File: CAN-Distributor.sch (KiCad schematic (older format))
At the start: 1 part

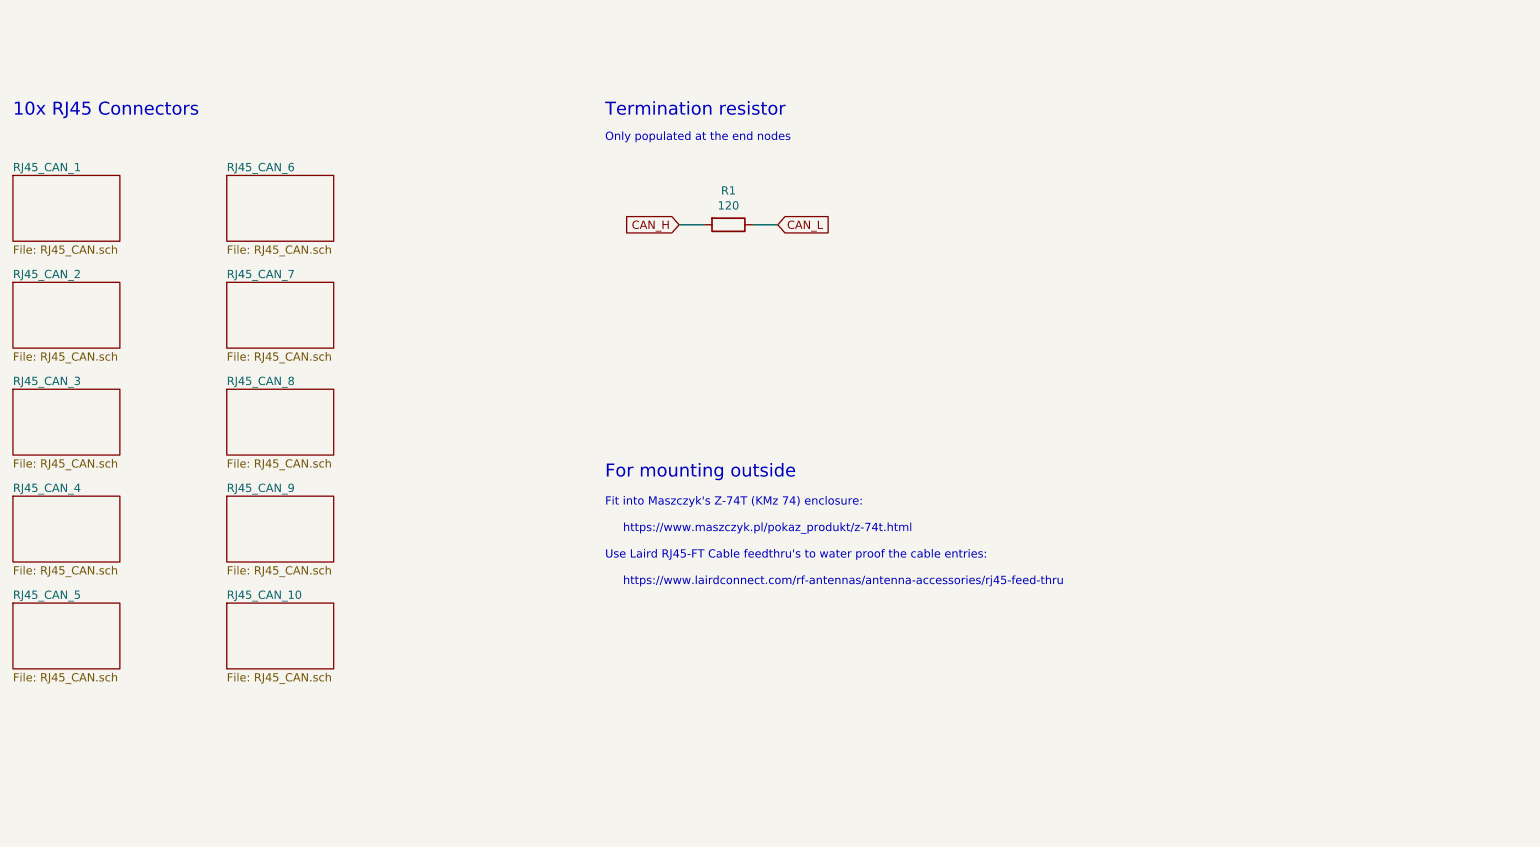
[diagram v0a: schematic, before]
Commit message: Design v2 circuit and make footprints.
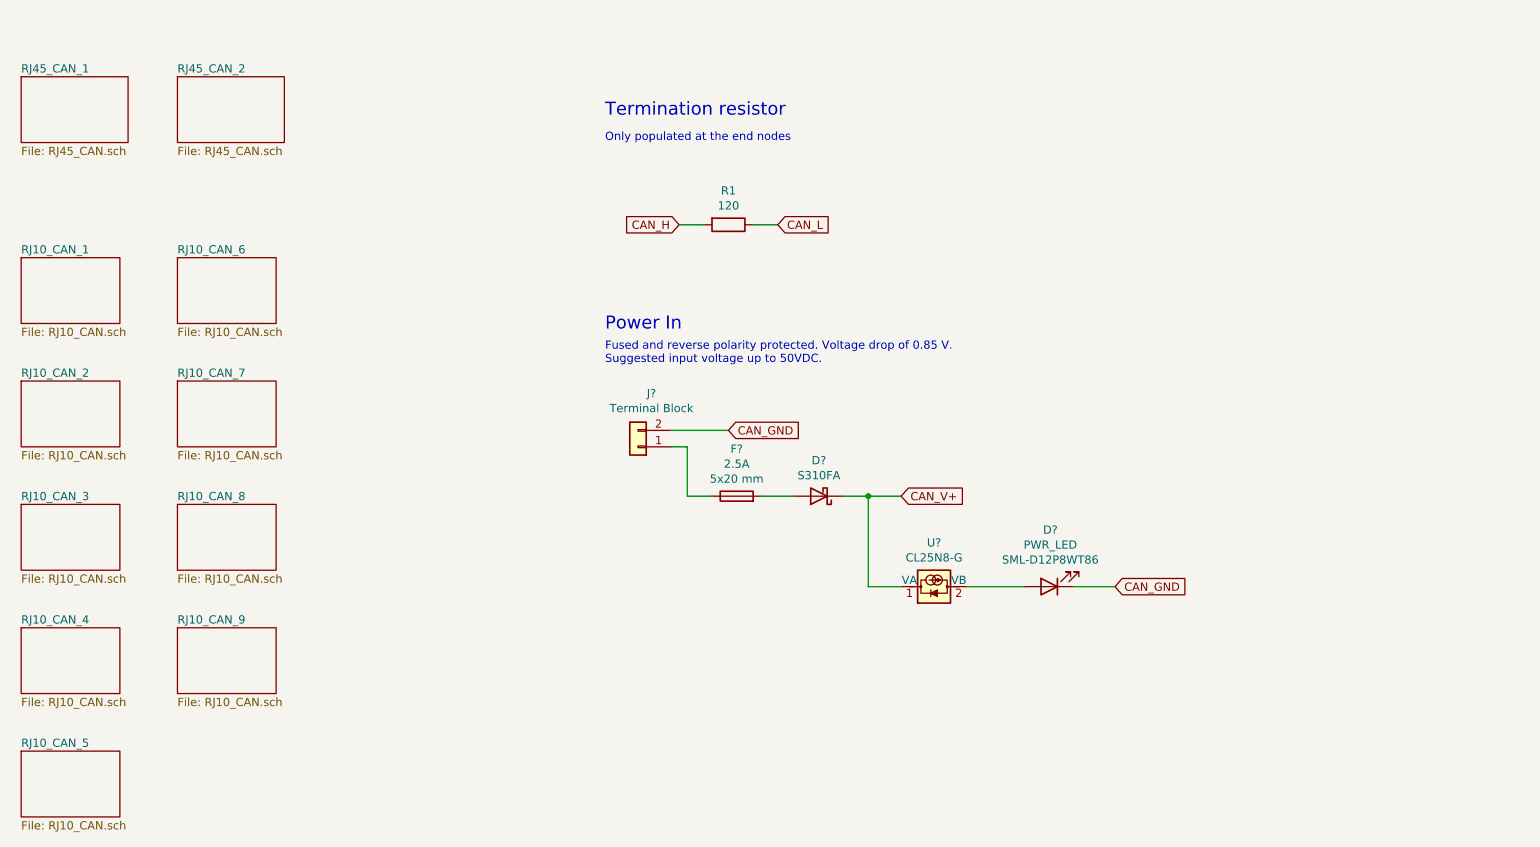
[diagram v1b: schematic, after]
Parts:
- added D?: D_Schottky, Diode_SMD:D_SOD-123F, symbol Device:D_Schottky
- added D?: PWR_LED, Diode_SMD:D_0603_1608Metric, symbol Device:LED
- added F?: 2.5A, Fuse:Fuseholder_Cylinder-5x20mm_Schurter_0031_8201_Horizontal_Open, symbol Device:Fuse
- added J?: Terminal Block, TerminalBlock:TerminalBlock_bornier-2_P5.08mm, symbol Connector_Generic:Conn_01x02
- added U?: CL25N8-G, Package_TO_SOT_SMD:SOT-89-3, symbol Driver_LED:CL220K4-G
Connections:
- new net: F?.1, J?.1 (Pin_1)
- new net: D?.2 (A), F?.2
- new net: D?.2 (A), U?.2 (VB)
- new net CAN_GND: D?.1 (K), J?.2 (Pin_2)
- new net CAN_V+: D?.1 (K), U?.1 (VA)
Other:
- note added: "Fused and reverse polarity protected. Voltage drop of 0.85 V. \nSuggested input voltage up to 50VDC."
- note added: "Power In"
- note removed: "10x RJ45 Connectors"
- note removed: "Fit into Maszczyk's Z-74T (KMz 74) enclosure:\n\n https://www.maszczyk.pl/pokaz_produkt/z-74t.html\n\nUse Laird RJ45-FT Cable feedthru's to water proof the cable entries:\n\n https://www.lairdconnect.com/rf-antennas/antenna-accessories/rj45-feed-thru"
- note removed: "For mounting outside"
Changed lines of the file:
@@
 $Descr A4 11693 8268
 encoding utf-8
-Sheet 1 11
+Sheet 1 12
 Title "CAN Distributor"
-Date "2021-02-26"
-Rev "1.0"
+Date "2021-04-03"
+Rev "2.0"
 Comp ""
 Comment1 "Designed by: Erik Almbratt"
@@
 $EndDescr
 $Sheet
-S 1650 2550 650  400
+S 1700 1950 650  400
 U 603ADFE4
 F0 "RJ45_CAN_1" 50
@@
 $EndSheet
 $Sheet
-S 1650 3200 650  400
+S 2650 1950 650  400
 U 603AF7FC
 F0 "RJ45_CAN_2" 50
 F1 "RJ45_CAN.sch" 50
 $EndSheet
-$Sheet
-S 1650 3850 650  400
-U 603AF88D
-F0 "RJ45_CAN_3" 50
-F1 "RJ45_CAN.sch" 50
-$EndSheet
-$Sheet
-S 1650 4500 650  400
-U 603AF8B1
-F0 "RJ45_CAN_4" 50
-F1 "RJ45_CAN.sch" 50
-$EndSheet
-$Sheet
-S 1650 5150 650  400
-U 603AF8D1
-F0 "RJ45_CAN_5" 50
-F1 "RJ45_CAN.sch" 50
-$EndSheet
-$Sheet
-S 2950 2550 650  400
-U 603AFD78
-F0 "RJ45_CAN_6" 50
-F1 "RJ45_CAN.sch" 50
-$EndSheet
-$Sheet
-S 2950 3200 650  400
-U 603AFD7A
-F0 "RJ45_CAN_7" 50
-F1 "RJ45_CAN.sch" 50
-$EndSheet
-$Sheet
-S 2950 3850 650  400
-U 603AFD7C
-F0 "RJ45_CAN_8" 50
-F1 "RJ45_CAN.sch" 50
-$EndSheet
-$Sheet
-S 2950 4500 650  400
-U 603AFD7E
-F0 "RJ45_CAN_9" 50
-F1 "RJ45_CAN.sch" 50
-$EndSheet
-$Sheet
-S 2950 5150 650  400
-U 603AFD80
-F0 "RJ45_CAN_10" 50
-F1 "RJ45_CAN.sch" 50
-$EndSheet
-Text Notes 1650 2200 0    79   ~ 0
-10x RJ45 Connectors
 $Comp
 L Device:R R1
@@
 F 2 "Resistor_THT:R_Axial_DIN0411_L9.9mm_D3.6mm_P15.24mm_Horizontal" V 5930 2850 50  0001 C CNN
 F 3 "~" H 6000 2850 50  0001 C CNN
+F 4 "~" H 6000 2850 50  0001 C CNN "Farnell"
+F 5 "~" H 6000 2850 50  0001 C CNN "MPN"
+F 6 "~" H 6000 2850 50  0001 C CNN "Manufacturer"
 	1    6000 2850
 	0    1    1    0
@@
 Text Notes 5250 2350 0    50   ~ 0
 Only populated at the end nodes
-Text Notes 5250 4400 0    79   ~ 0
-For mounting outside
-Text Notes 5250 5050 0    50   ~ 0
-Fit into Maszczyk's Z-74T (KMz 74) enclosure:\n\n     https://www.maszczyk.pl/pokaz_produkt/z-74t.html\n\nUse Laird RJ45-FT Cable feedthru's to water proof the cable entries:\n\n     https://www.lairdconnect.com/rf-antennas/antenna-accessories/rj45-feed-thru
+$Sheet
+S 1700 3050 600  400
+U 60682F6E
+F0 "RJ10_CAN_1" 50
+F1 "RJ10_CAN.sch" 50
+$EndSheet
+Text Notes 5250 3500 0    79   ~ 0
+Power In
+$Comp
+L Connector_Generic:Conn_01x02 J?
+U 1 1 60687EFE
+P 5450 4200
+F 0 "J?" H 5368 3875 50  0000 C CNN
+F 1 "Terminal Block" H 5368 3966 50  0000 C CNN
+F 2 "TerminalBlock:TerminalBlock_bornier-2_P5.08mm" H 5450 4200 50  0001 C CNN
+F 3 "~" H 5450 4200 50  0001 C CNN
+F 4 "~" H 5450 4200 50  0001 C CNN "Farnell"
+F 5 "~" H 5450 4200 50  0001 C CNN "MPN"
+F 6 "~" H 5450 4200 50  0001 C CNN "Manufacturer"
+	1    5450 4200
+	-1   0    0    1
+$EndComp
+Text GLabel 6000 4100 2    50   Input ~ 0
+CAN_GND
+Wire Wire Line
+	5650 4100 6000 4100
+Text GLabel 7050 4500 2    50   Input ~ 0
+CAN_V+
+Wire Wire Line
+	7050 4500 6850 4500
+$Comp
+L Device:Fuse F?
+U 1 1 60688CEC
+P 6050 4500
+F 0 "F?" V 6337 4500 50  0000 C CNN
+F 1 "2.5A" V 6246 4500 50  0000 C CNN
+F 2 "Fuse:Fuseholder_Cylinder-5x20mm_Schurter_0031_8201_Horizontal_Open" V 5980 4500 50  0001 C CNN
+F 3 "http://www.farnell.com/datasheets/2343287.pdf" H 6050 4500 50  0001 C CNN
+F 4 "0031.8201" V 6050 4500 50  0001 C CNN "MPN"
+F 5 "SCHURTER" V 6050 4500 50  0001 C CNN "Manufacturer"
+F 6 "5x20 mm" V 6155 4500 50  0000 C CNN "Description"
+F 7 "1162740" H 6050 4500 50  0001 C CNN "Farnell"
+	1    6050 4500
+	0    -1   -1   0
+$EndComp
+Wire Wire Line
+	5650 4200 5750 4200
+Wire Wire Line
+	5750 4200 5750 4500
+Wire Wire Line
+	5750 4500 5900 4500
+$Comp
+L Device:D_Schottky D?
+U 1 1 6068A695
+P 6550 4500
+F 0 "D?" H 6550 4283 50  0000 C CNN
+F 1 "D_Schottky" H 6550 4374 50  0001 C CNN
+F 2 "Diode_SMD:D_SOD-123F" H 6550 4500 50  0001 C CNN
+F 3 "https://datasheet.octopart.com/S310FA-ON-Semiconductor-datasheet-137362515.pdf" H 6550 4500 50  0001 C CNN
+F 4 "S310FA" H 6550 4374 50  0000 C CNN "MPN"
+F 5 "ON Semiconductor" H 6550 4500 50  0001 C CNN "Manufacturer"
+F 6 "" H 6550 4500 50  0001 C CNN "Description"
+F 7 "2822559" H 6550 4500 50  0001 C CNN "Farnell"
+	1    6550 4500
+	-1   0    0    1
+$EndComp
+Wire Wire Line
+	6200 4500 6400 4500
+$Comp
+L Device:LED D?
+U 1 1 6068B76E
+P 7950 5050
+F 0 "D?" H 7943 4705 50  0000 C CNN
+F 1 "PWR_LED" H 7943 4796 50  0000 C CNN
+F 2 "Diode_SMD:D_0603_1608Metric" H 7950 5050 50  0001 C CNN
+F 3 "https://datasheet.octopart.com/SML-D12P8WT86-Rohm-datasheet-142144708.pdf" H 7950 5050 50  0001 C CNN
+F 4 "SML-D12P8WT86" H 7943 4887 50  0000 C CNN "MPN"
+F 5 "ROHM" H 7950 5050 50  0001 C CNN "Manufacturer"
+F 6 "2687486" H 7950 5050 50  0001 C CNN "Farnell"
+	1    7950 5050
+	-1   0    0    1
+$EndComp
+Connection ~ 6850 4500
+Wire Wire Line
+	6850 4500 6700 4500
+Text GLabel 8350 5050 2    50   Input ~ 0
+CAN_GND
+Wire Wire Line
+	8350 5050 8100 5050
+$Comp
+L Driver_LED:CL220K4-G U?
+U 1 1 6068FB57
+P 7250 5050
+F 0 "U?" V 7517 5050 50  0000 C CNN
+F 1 "CL25N8-G" V 7426 5050 50  0001 C CNN
+F 2 "Package_TO_SOT_SMD:SOT-89-3" H 7400 5000 50  0001 L CNN
+F 3 "http://www.farnell.com/datasheets/1849619.pdf" H 7260 5050 50  0001 C CNN
+F 4 "CL25N8-G" V 7426 5050 50  0000 C CNN "MPN"
+F 5 "Microchip" H 7250 5050 50  0001 C CNN "Manufacturer"
+F 6 "2448489" H 7250 5050 50  0001 C CNN "Farnell"
+	1    7250 5050
+	0    -1   -1   0
+$EndComp
+Wire Wire Line
+	6850 4500 6850 5050
+Wire Wire Line
+	7050 5050 6850 5050
+Text Notes 5250 3700 0    50   ~ 0
+Fused and reverse polarity protected. Voltage drop of 0.85 V. \nSuggested input voltage up to 50VDC.
+Wire Wire Line
+	7450 5050 7800 5050
+$Sheet
+S 1700 3800 600  400
+U 6069ABE0
+F0 "RJ10_CAN_2" 50
+F1 "RJ10_CAN.sch" 50
+$EndSheet
+$Sheet
+S 1700 4550 600  400
+U 6069AD3C
+F0 "RJ10_CAN_3" 50
+F1 "RJ10_CAN.sch" 50
+$EndSheet
+$Sheet
+S 1700 5300 600  400
+U 6069AD3E
+F0 "RJ10_CAN_4" 50
+F1 "RJ10_CAN.sch" 50
+$EndSheet
+$Sheet
+S 1700 6050 600  400
+U 6069AE53
+F0 "RJ10_CAN_5" 50
+F1 "RJ10_CAN.sch" 50
+$EndSheet
+$Sheet
+S 2650 3050 600  400
+U 6069B12F
+F0 "RJ10_CAN_6" 50
+F1 "RJ10_CAN.sch" 50
+$EndSheet
+$Sheet
+S 2650 3800 600  400
+U 6069B131
+F0 "RJ10_CAN_7" 50
+F1 "RJ10_CAN.sch" 50
+$EndSheet
+$Sheet
+S 2650 4550 600  400
+U 6069B133
+F0 "RJ10_CAN_8" 50
+F1 "RJ10_CAN.sch" 50
+$EndSheet
+$Sheet
+S 2650 5300 600  400
+U 6069B135
+F0 "RJ10_CAN_9" 50
+F1 "RJ10_CAN.sch" 50
+$EndSheet
 $EndSCHEMATC

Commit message: Perform layout. Add CAN testpoints.
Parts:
- J1: renamed from J?; value Terminal Block -> 2p Terminal Block
- gave numbers to parts that had none: 4
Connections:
- net CAN_GND: now also J1.1 (Pin_1); no longer J1.2 (Pin_2)
- net at F1.1: now also J1.2 (Pin_2); no longer J1.1 (Pin_1)
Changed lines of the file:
@@
 $Descr A4 11693 8268
 encoding utf-8
-Sheet 1 12
+Sheet 1 16
 Title "CAN Distributor"
 Date "2021-04-03"
@@
 Power In
 $Comp
-L Connector_Generic:Conn_01x02 J?
+L Connector_Generic:Conn_01x02 J1
 U 1 1 60687EFE
-P 5450 4200
-F 0 "J?" H 5368 3875 50  0000 C CNN
-F 1 "Terminal Block" H 5368 3966 50  0000 C CNN
-F 2 "TerminalBlock:TerminalBlock_bornier-2_P5.08mm" H 5450 4200 50  0001 C CNN
-F 3 "~" H 5450 4200 50  0001 C CNN
-F 4 "~" H 5450 4200 50  0001 C CNN "Farnell"
-F 5 "~" H 5450 4200 50  0001 C CNN "MPN"
-F 6 "~" H 5450 4200 50  0001 C CNN "Manufacturer"
-	1    5450 4200
-	-1   0    0    1
+P 5450 4100
+F 0 "J1" H 5368 4317 50  0000 C CNN
+F 1 "2p Terminal Block" H 5368 4226 50  0000 C CNN
+F 2 "TerminalBlock:TerminalBlock_bornier-2_P5.08mm" H 5450 4100 50  0001 C CNN
+F 3 "~" H 5450 4100 50  0001 C CNN
+F 4 "~" H 5450 4100 50  0001 C CNN "Farnell"
+F 5 "~" H 5450 4100 50  0001 C CNN "MPN"
+F 6 "~" H 5450 4100 50  0001 C CNN "Manufacturer"
+	1    5450 4100
+	-1   0    0    -1
 $EndComp
 Text GLabel 6000 4100 2    50   Input ~ 0
@@
 	7050 4500 6850 4500
 $Comp
-L Device:Fuse F?
+L Device:Fuse F1
 U 1 1 60688CEC
 P 6050 4500
-F 0 "F?" V 6337 4500 50  0000 C CNN
+F 0 "F1" V 6337 4500 50  0000 C CNN
 F 1 "2.5A" V 6246 4500 50  0000 C CNN
 F 2 "Fuse:Fuseholder_Cylinder-5x20mm_Schurter_0031_8201_Horizontal_Open" V 5980 4500 50  0001 C CNN
@@
 	5750 4500 5900 4500
 $Comp
-L Device:D_Schottky D?
+L Device:D_Schottky D1
 U 1 1 6068A695
 P 6550 4500
-F 0 "D?" H 6550 4283 50  0000 C CNN
+F 0 "D1" H 6550 4283 50  0000 C CNN
 F 1 "D_Schottky" H 6550 4374 50  0001 C CNN
 F 2 "Diode_SMD:D_SOD-123F" H 6550 4500 50  0001 C CNN
@@
 	6200 4500 6400 4500
 $Comp
-L Device:LED D?
+L Device:LED D2
 U 1 1 6068B76E
 P 7950 5050
-F 0 "D?" H 7943 4705 50  0000 C CNN
+F 0 "D2" H 7943 4705 50  0000 C CNN
 F 1 "PWR_LED" H 7943 4796 50  0000 C CNN
 F 2 "Diode_SMD:D_0603_1608Metric" H 7950 5050 50  0001 C CNN
@@
 	8350 5050 8100 5050
 $Comp
-L Driver_LED:CL220K4-G U?
+L Driver_LED:CL220K4-G U1
 U 1 1 6068FB57
 P 7250 5050
-F 0 "U?" V 7517 5050 50  0000 C CNN
+F 0 "U1" V 7517 5050 50  0000 C CNN
 F 1 "CL25N8-G" V 7426 5050 50  0001 C CNN
 F 2 "Package_TO_SOT_SMD:SOT-89-3" H 7400 5000 50  0001 L CNN
@@
 F1 "RJ10_CAN.sch" 50
 $EndSheet
+$Sheet
+S 3900 5300 600  400
+U 606A6B6A
+F0 "TP_CAN_1" 50
+F1 "TP_CAN9.sch" 50
+$EndSheet
+$Sheet
+S 3900 6050 600  400
+U 606A6E99
+F0 "TP_CAN_2" 50
+F1 "TP_CAN9.sch" 50
+$EndSheet
+$Sheet
+S 4850 5300 600  400
+U 606A6FCD
+F0 "TP_CAN_3" 50
+F1 "TP_CAN9.sch" 50
+$EndSheet
+$Sheet
+S 4850 6050 600  400
+U 606A70AE
+F0 "TP_CAN_4" 50
+F1 "TP_CAN9.sch" 50
+$EndSheet
 $EndSCHEMATC

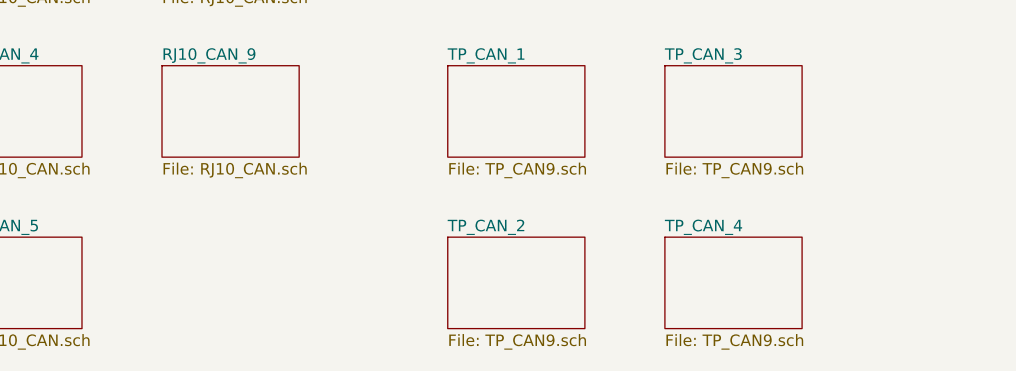
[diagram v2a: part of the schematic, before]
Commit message: Add a tenth RJ10 connector.
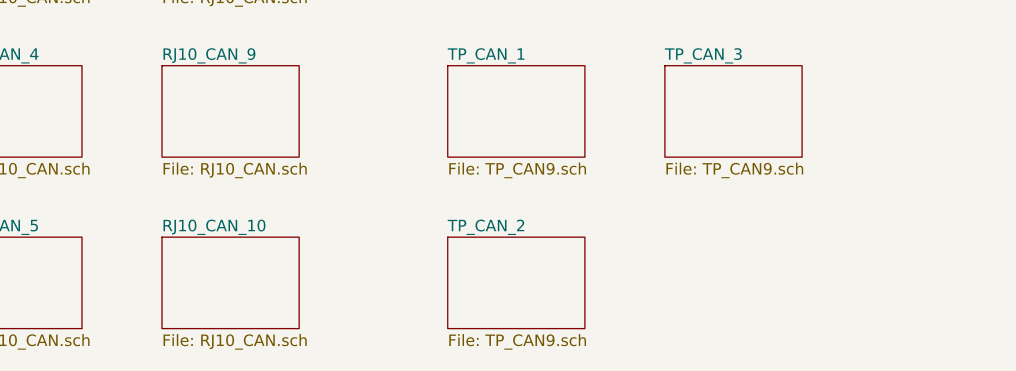
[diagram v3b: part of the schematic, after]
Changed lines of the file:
@@
 Wire Wire Line
 	6150 2850 6300 2850
-Text Notes 5250 2200 0    79   ~ 0
-Termination resistor
 Text Notes 5250 2350 0    50   ~ 0
 Only populated at the end nodes
@@
 F1 "TP_CAN9.sch" 50
 $EndSheet
+Text Notes 5250 2200 0    79   ~ 0
+Termination resistor
 $Sheet
-S 4850 6050 600  400
-U 606A70AE
-F0 "TP_CAN_4" 50
-F1 "TP_CAN9.sch" 50
+S 2650 6050 600  400
+U 606AA4F3
+F0 "RJ10_CAN_10" 50
+F1 "RJ10_CAN.sch" 50
 $EndSheet
 $EndSCHEMATC
